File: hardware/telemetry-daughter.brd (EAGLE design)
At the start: 47.2 x 56 mm, 18 parts, among them J1 I2C, J2 MICRO-SD_CARD_SOCKET, J3 IO, J4 TEMP, J5 GPS1, U2 DNP

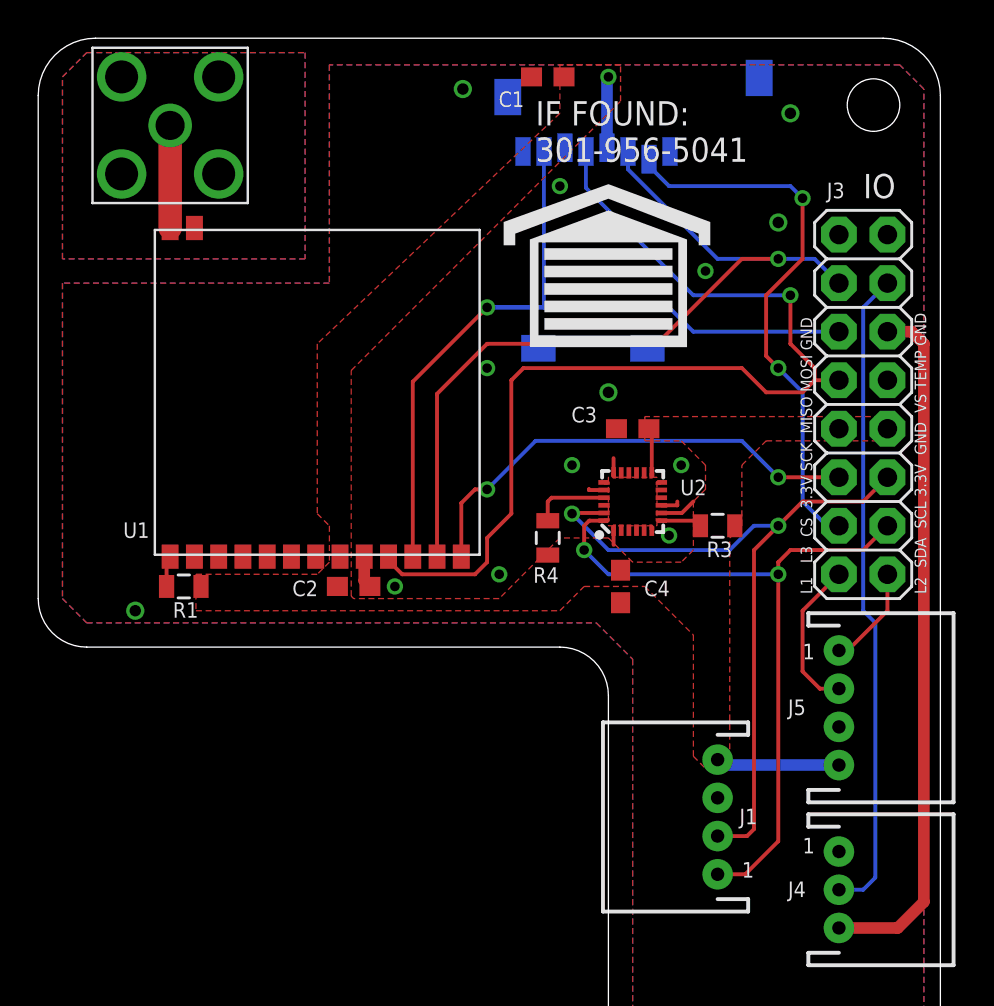
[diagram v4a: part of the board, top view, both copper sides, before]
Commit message: Change LoRA footprint on daughter card to the RA-02 which is easier to obtain
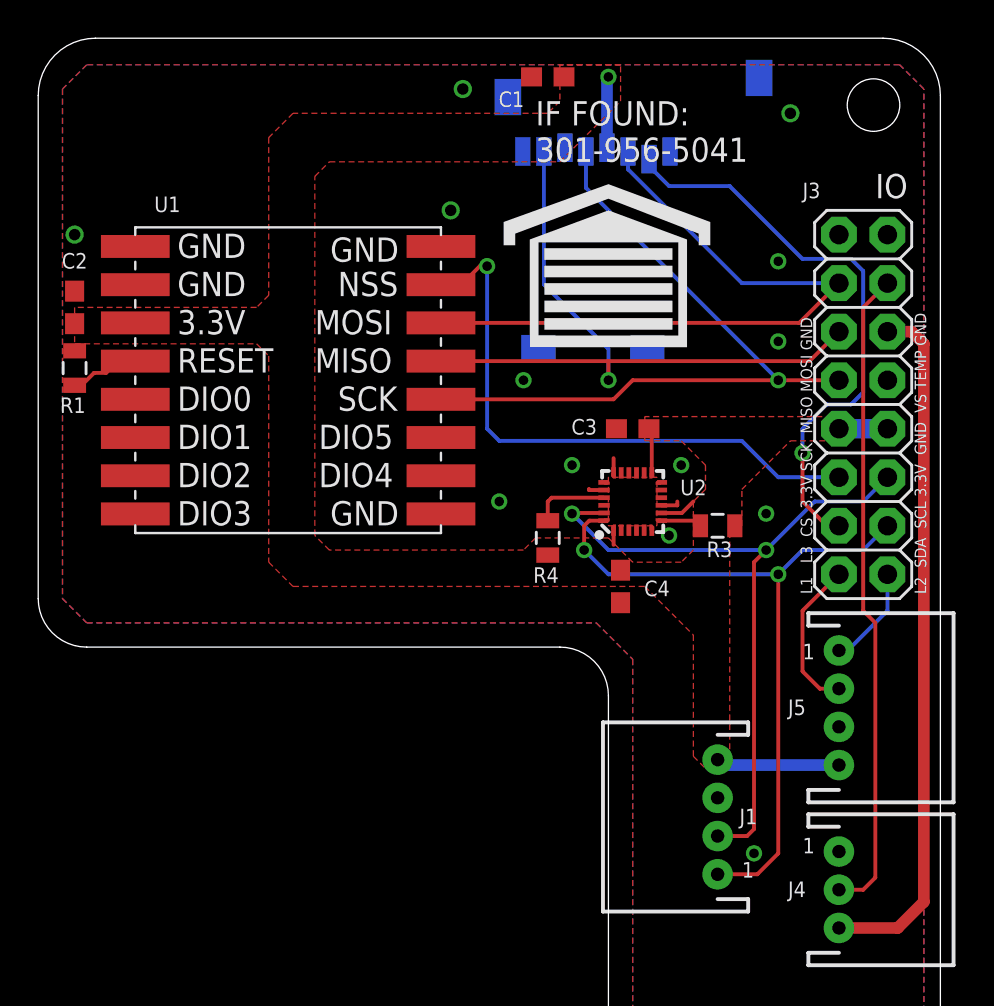
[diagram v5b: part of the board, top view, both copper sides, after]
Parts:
- removed U$3: SMA_VERT, HAB:SMA_VERT
- U1: value (none) -> RA02; device HAB:DRF1278F -> HAB:RA02
- moved C2 20.7 mm to (19.7, 41.9), turned to 90 degrees
- moved R1 12.8 mm to (19.7, 38.7), turned to 270 degrees
- moved U1 1.65 mm to (30.9, 38.1), turned to 0 degrees
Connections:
- removed net RF_LORA: U$3.P$1, U1.15
- removed net RGND: U$3.P$2, U$3.P$3, U$3.P$4, U$3.P$5, U1.14
- net !LORA_CS!: now also U1.15; no longer U1.13
- net !LORA_RST!: now also U1.4; no longer U1.1
- net !L_INT!: now also U1.5; no longer U1.2
- net 3.3V: now also U1.3; no longer U1.8
- net GND: now also U1.1, U1.16, U1.2
- net MISO: now also U1.13; no longer U1.11
- net MOSI: now also U1.14; no longer U1.12
- net SCK: now also U1.12; no longer U1.10
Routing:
- net SCK: track 54.1 -> 37.4 mm
- net MISO: track 44.7 -> 35.8 mm
- net MOSI: track 43.7 -> 36.1 mm, vias 1 -> 0
- net !LORA_CS!: track 24.7 -> 30.8 mm, vias 2 -> 1
- net RF_LORA: track 5.37 -> 0.00 mm
- net 3.3V: track 15.2 -> 17.7 mm
- net !LORA_RST!: track 1.74 -> 3.70 mm
- net GND: track 4.28 -> 2.60 mm
- net SCL: track 39.0 -> 37.5 mm
- net !SD_CS!: track 29.0 -> 30.4 mm, vias 2 -> 1
- removed copper zone on layer 1, net RGND
- removed copper zone on layer 16, net RGND
